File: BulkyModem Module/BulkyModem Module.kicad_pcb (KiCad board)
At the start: 2 copper layers, 100 x 100 mm, 93 parts, among them J1 DC IN, J2 DCE, J3 Module_Panel, J4 Conn_Power, J5 C64_Modem_IDC, K1 HK19F-DC, M1 Mounting, M2 Mounting, M3 Mounting, M4 Mounting, Q1 2N3904, Q4 2N3904, Q5 2N3904, Q6 2N3904, Q7 2N3904, Q8 2N3904, U1 74HCT244, U2 74HCT04, U3 MAX232, U4 MAX232, U5 74HCT04

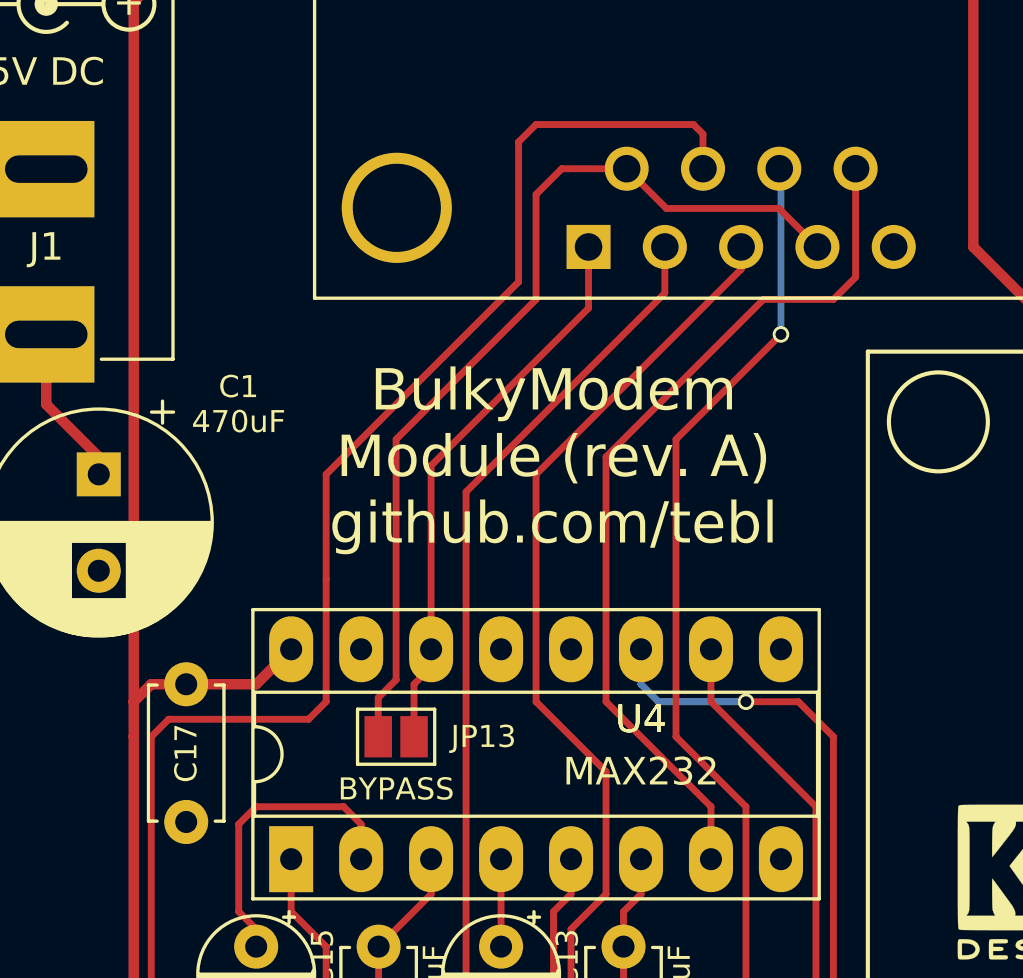
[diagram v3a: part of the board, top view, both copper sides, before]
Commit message: Tweak schematic in order to fix LEDs and default jumper settings moved to working configuration
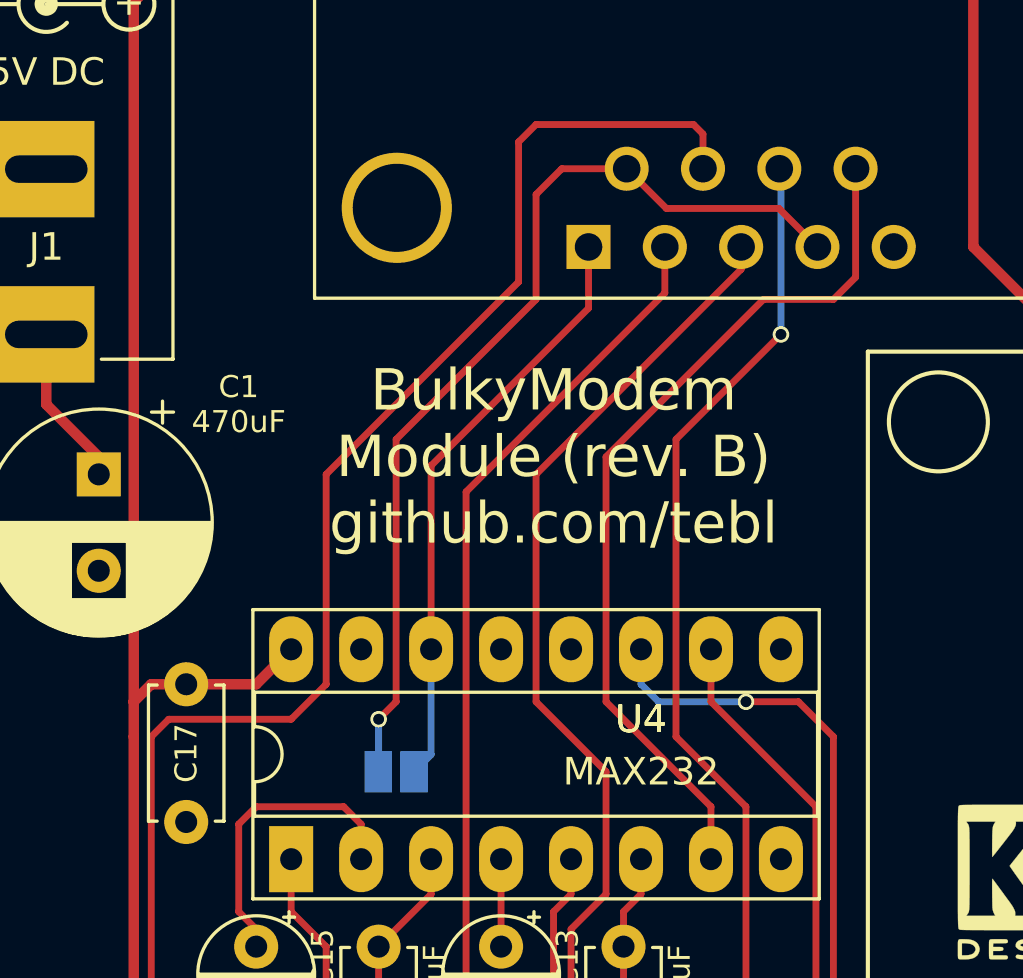
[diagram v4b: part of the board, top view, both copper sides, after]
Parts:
- JP13: moved to B.Cu
- moved JP13 1.27 mm to (95.9, 84.5)
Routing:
- net Net-(J2-Pad4): track 33.8 -> 35.1 mm, vias 0 -> 1
- net /RS-232/SER_DCD: track 20.4 -> 21.7 mm
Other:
- board text added: "BulkyModem Module (rev. B) github.com/tebl"
- board text removed: "BulkyModem Module (rev. A) github.com/tebl"
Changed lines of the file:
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@@
       (net 78 "Net-(JP12-Pad2)"))
   )
-  (module Jumper:SolderJumper-2_P1.3mm_Open_Pad1.0x1.5mm (layer F.Cu)
-    (at 95.885 83.185 180)
+  (module Jumper:SolderJumper-2_P1.3mm_Open_Pad1.0x1.5mm (layer B.Cu)
+    (at 95.885 84.455 180)
     (descr "SMD Solder Jumper, 1x1.5mm Pads, 0.3mm gap, open")
     (tags "solder jumper open")
     (attr virtual)
-    (fp_text reference JP13 (at -3.175 0) (layer F.SilkS)
-      (effects (font (size 0.8 0.8) (thickness 0.1)))
-    )
-    (fp_text value BYPASS (at 0 -1.905) (layer F.SilkS)
-      (effects (font (size 0.8 0.8) (thickness 0.1)))
-    )
-    (fp_line (start -1.4 1) (end -1.4 -1) (layer F.SilkS) (width 0.12))
-    (fp_line (start 1.4 1) (end -1.4 1) (layer F.SilkS) (width 0.12))
-    (fp_line (start 1.4 -1) (end 1.4 1) (layer F.SilkS) (width 0.12))
-    (fp_line (start -1.4 -1) (end 1.4 -1) (layer F.SilkS) (width 0.12))
-    (fp_line (start -1.65 -1.25) (end 1.65 -1.25) (layer F.CrtYd) (width 0.05))
-    (fp_line (start -1.65 -1.25) (end -1.65 1.25) (layer F.CrtYd) (width 0.05))
-    (fp_line (start 1.65 1.25) (end 1.65 -1.25) (layer F.CrtYd) (width 0.05))
-    (fp_line (start 1.65 1.25) (end -1.65 1.25) (layer F.CrtYd) (width 0.05))
-    (pad 2 smd rect (at 0.65 0 180) (size 1 1.5) (layers F.Cu F.Mask)
+    (fp_text reference JP13 (at -3.175 0) (layer B.SilkS)
+      (effects (font (size 0.8 0.8) (thickness 0.1)) (justify mirror))
+    )
+    (fp_text value BYPASS (at 0 1.905) (layer B.SilkS)
+      (effects (font (size 0.8 0.8) (thickness 0.1)) (justify mirror))
+    )
+    (fp_line (start -1.4 -1) (end -1.4 1) (layer B.SilkS) (width 0.12))
+    (fp_line (start 1.4 -1) (end -1.4 -1) (layer B.SilkS) (width 0.12))
+    (fp_line (start 1.4 1) (end 1.4 -1) (layer B.SilkS) (width 0.12))
+    (fp_line (start -1.4 1) (end 1.4 1) (layer B.SilkS) (width 0.12))
+    (fp_line (start -1.65 1.25) (end 1.65 1.25) (layer B.CrtYd) (width 0.05))
+    (fp_line (start -1.65 1.25) (end -1.65 -1.25) (layer B.CrtYd) (width 0.05))
+    (fp_line (start 1.65 -1.25) (end 1.65 1.25) (layer B.CrtYd) (width 0.05))
+    (fp_line (start 1.65 -1.25) (end -1.65 -1.25) (layer B.CrtYd) (width 0.05))
+    (pad 2 smd rect (at 0.65 0 180) (size 1 1.5) (layers B.Cu B.Mask)
       (net 76 "Net-(J2-Pad4)"))
-    (pad 1 smd rect (at -0.65 0 180) (size 1 1.5) (layers F.Cu F.Mask)
+    (pad 1 smd rect (at -0.65 0 180) (size 1 1.5) (layers B.Cu B.Mask)
       (net 75 /RS-232/SER_DCD))
   )
@@
     (effects (font (size 1 1) (thickness 0.15)))
   )
-  (gr_text "BulkyModem\nModule (rev. A)\ngithub.com/tebl" (at 101.6 73.025) (layer F.SilkS)
+  (gr_text "BulkyModem\nModule (rev. B)\ngithub.com/tebl" (at 101.6 73.025) (layer F.SilkS)
     (effects (font (size 1.5 1.5) (thickness 0.15)))
   )
@@
   (segment (start 102.235 90.17) (end 102.235 92.71) (width 0.25) (layer F.Cu) (net 36))
   (segment (start 108.41 65.405) (end 108.41 66.215) (width 0.25) (layer F.Cu) (net 36) (status 10))
-  (segment (start 107.025 62.565) (end 107.025 61.305) (width 0.25) (layer F.Cu) (net 37) (status 10))
-  (segment (start 107.025 61.305) (end 106.68 60.96) (width 0.25) (layer F.Cu) (net 37))
-  (segment (start 106.68 60.96) (end 100.965 60.96) (width 0.25) (layer F.Cu) (net 37))
-  (segment (start 100.965 60.96) (end 100.33 61.595) (width 0.25) (layer F.Cu) (net 37))
-  (segment (start 100.33 61.595) (end 100.33 66.675) (width 0.25) (layer F.Cu) (net 37))
-  (segment (start 100.33 66.675) (end 93.345 73.66) (width 0.25) (layer F.Cu) (net 37))
-  (segment (start 93.345 73.66) (end 93.345 77.47) (width 0.25) (layer F.Cu) (net 37))
-  (segment (start 93.345 77.47) (end 93.345 81.915) (width 0.25) (layer F.Cu) (net 37))
-  (segment (start 109.22 122.555) (end 109.22 121.285) (width 0.25) (layer F.Cu) (net 37) (status 20))
+  (segment (start 109.22 122.555) (end 109.22 121.285) (width 0.25) (layer F.Cu) (net 37))
   (segment (start 108.585 123.19) (end 109.22 122.555) (width 0.25) (layer F.Cu) (net 37))
   (segment (start 106.68 123.19) (end 108.585 123.19) (width 0.25) (layer F.Cu) (net 37))
   (segment (start 106.045 122.555) (end 106.68 123.19) (width 0.25) (layer F.Cu) (net 37))
+  (segment (start 93.98 109.22) (end 105.41 109.22) (width 0.25) (layer F.Cu) (net 37))
+  (segment (start 93.345 108.585) (end 93.98 109.22) (width 0.25) (layer F.Cu) (net 37))
+  (segment (start 93.345 105.41) (end 93.345 108.585) (width 0.25) (layer F.Cu) (net 37))
+  (segment (start 91.694 94.234) (end 92.71 95.25) (width 0.25) (layer F.Cu) (net 37))
+  (segment (start 107.025 61.305) (end 106.68 60.96) (width 0.25) (layer F.Cu) (net 37))
+  (segment (start 92.71 104.775) (end 93.345 105.41) (width 0.25) (layer F.Cu) (net 37))
+  (segment (start 100.33 61.595) (end 100.33 66.675) (width 0.25) (layer F.Cu) (net 37))
+  (segment (start 107.025 62.565) (end 107.025 61.305) (width 0.25) (layer F.Cu) (net 37))
+  (segment (start 93.345 81.28) (end 92.075 82.55) (width 0.25) (layer F.Cu) (net 37))
+  (segment (start 100.965 60.96) (end 100.33 61.595) (width 0.25) (layer F.Cu) (net 37))
+  (segment (start 106.68 60.96) (end 100.965 60.96) (width 0.25) (layer F.Cu) (net 37))
+  (segment (start 92.075 82.55) (end 87.63 82.55) (width 0.25) (layer F.Cu) (net 37))
+  (segment (start 105.41 109.22) (end 106.045 109.855) (width 0.25) (layer F.Cu) (net 37))
+  (segment (start 100.33 66.675) (end 93.345 73.66) (width 0.25) (layer F.Cu) (net 37))
+  (segment (start 93.345 73.66) (end 93.345 81.28) (width 0.25) (layer F.Cu) (net 37))
+  (segment (start 92.71 95.25) (end 92.71 104.775) (width 0.25) (layer F.Cu) (net 37))
+  (segment (start 87.63 82.55) (end 86.995 83.185) (width 0.25) (layer F.Cu) (net 37))
+  (segment (start 86.995 83.185) (end 86.995 93.345) (width 0.25) (layer F.Cu) (net 37))
+  (segment (start 87.884 94.234) (end 91.694 94.234) (width 0.25) (layer F.Cu) (net 37))
   (segment (start 106.045 109.855) (end 106.045 122.555) (width 0.25) (layer F.Cu) (net 37))
-  (segment (start 93.345 81.915) (end 92.71 82.55) (width 0.25) (layer F.Cu) (net 37))
-  (segment (start 93.345 105.41) (end 93.345 108.585) (width 0.25) (layer F.Cu) (net 37))
-  (segment (start 92.71 82.55) (end 87.63 82.55) (width 0.25) (layer F.Cu) (net 37))
-  (segment (start 86.995 83.185) (end 86.995 93.345) (width 0.25) (layer F.Cu) (net 37))
   (segment (start 86.995 93.345) (end 87.884 94.234) (width 0.25) (layer F.Cu) (net 37))
-  (segment (start 87.63 82.55) (end 86.995 83.185) (width 0.25) (layer F.Cu) (net 37))
-  (segment (start 91.694 94.234) (end 92.71 95.25) (width 0.25) (layer F.Cu) (net 37))
-  (segment (start 87.884 94.234) (end 91.694 94.234) (width 0.25) (layer F.Cu) (net 37))
-  (segment (start 92.71 95.25) (end 92.71 104.775) (width 0.25) (layer F.Cu) (net 37))
-  (segment (start 93.345 108.585) (end 93.98 109.22) (width 0.25) (layer F.Cu) (net 37))
-  (segment (start 92.71 104.775) (end 93.345 105.41) (width 0.25) (layer F.Cu) (net 37))
-  (segment (start 105.41 109.22) (end 106.045 109.855) (width 0.25) (layer F.Cu) (net 37))
-  (segment (start 93.98 109.22) (end 105.41 109.22) (width 0.25) (layer F.Cu) (net 37))
   (via (at 109.855 68.58) (size 0.6) (drill 0.4) (layers F.Cu B.Cu) (net 38))
   (segment (start 109.855 62.625) (end 109.795 62.565) (width 0.25) (layer B.Cu) (net 38) (status 30))
@@
   (segment (start 97.155 73.3425) (end 102.87 67.6275) (width 0.25) (layer F.Cu) (net 75))
   (segment (start 97.155 80.01) (end 97.155 73.3425) (width 0.25) (layer F.Cu) (net 75) (status 10))
-  (segment (start 97.155 80.66) (end 97.155 80.01) (width 0.25) (layer F.Cu) (net 75) (status 30))
-  (segment (start 96.535 81.28) (end 97.155 80.66) (width 0.25) (layer F.Cu) (net 75) (status 20))
-  (segment (start 96.535 81.28) (end 96.535 83.185) (width 0.25) (layer F.Cu) (net 75) (status 20))
+  (segment (start 97.155 83.835) (end 96.535 84.455) (width 0.25) (layer B.Cu) (net 75))
+  (segment (start 97.155 80.01) (end 97.155 83.835) (width 0.25) (layer B.Cu) (net 75))
   (segment (start 109.783 64.008) (end 111.18 65.405) (width 0.25) (layer F.Cu) (net 76) (status 20))
   (segment (start 105.698 64.008) (end 109.783 64.008) (width 0.25) (layer F.Cu) (net 76))
   (segment (start 104.255 62.565) (end 105.698 64.008) (width 0.25) (layer F.Cu) (net 76) (status 10))
-  (segment (start 101.9 62.565) (end 104.255 62.565) (width 0.25) (layer F.Cu) (net 76) (status 20))
-  (segment (start 100.965 63.5) (end 101.9 62.565) (width 0.25) (layer F.Cu) (net 76))
-  (segment (start 100.965 67.31) (end 100.965 63.5) (width 0.25) (layer F.Cu) (net 76))
-  (segment (start 95.885 72.39) (end 100.965 67.31) (width 0.25) (layer F.Cu) (net 76))
-  (segment (start 95.885 81.12125) (end 95.885 72.39) (width 0.25) (layer F.Cu) (net 76))
-  (segment (start 95.235 81.77125) (end 95.885 81.12125) (width 0.25) (layer F.Cu) (net 76))
-  (segment (start 95.235 83.185) (end 95.235 81.77125) (width 0.25) (layer F.Cu) (net 76) (status 10))
+  (via (at 95.25 82.55) (size 0.6) (drill 0.4) (layers F.Cu B.Cu) (net 76))
+  (segment (start 95.25 84.44) (end 95.235 84.455) (width 0.25) (layer B.Cu) (net 76))
+  (segment (start 95.25 82.55) (end 95.25 84.44) (width 0.25) (layer B.Cu) (net 76))
+  (segment (start 95.885 81.915) (end 95.25 82.55) (width 0.25) (layer F.Cu) (net 76))
+  (segment (start 95.885 72.39) (end 95.885 81.915) (width 0.25) (layer F.Cu) (net 76))
+  (segment (start 100.965 67.31) (end 95.885 72.39) (width 0.25) (layer F.Cu) (net 76))
+  (segment (start 100.965 63.5) (end 100.965 67.31) (width 0.25) (layer F.Cu) (net 76))
+  (segment (start 101.9 62.565) (end 100.965 63.5) (width 0.25) (layer F.Cu) (net 76))
+  (segment (start 104.255 62.565) (end 101.9 62.565) (width 0.25) (layer F.Cu) (net 76))
   (segment (start 129.57 106.65) (end 129.54 106.68) (width 0.25) (layer F.Cu) (net 77) (status 30))
   (segment (start 129.57 103.505) (end 129.57 106.65) (width 0.25) (layer F.Cu) (net 77) (status 30))

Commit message: Layout updated
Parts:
- removed C10, C11, C16, C20, C9: 22uF, Capacitor_THT:CP_Radial_D5.0mm_P2.00mm
- removed the G*** at (79.4, 113.0)
- removed J4: Conn_Power, BulkyModem:Conn_Power
- removed Q1, Q4, Q5, Q6, Q7, Q8: 2N3904, Package_TO_SOT_THT:TO-92_Inline_Wide
- removed R11, R13, R24, R7, R9: 10k, resistor:R_Axial_DIN0207_L6.3mm_D2.5mm_P10.16mm_Horizontal
- removed R22: 2k, resistor:R_Axial_DIN0207_L6.3mm_D2.5mm_P10.16mm_Horizontal
- removed R23: 1k, resistor:R_Axial_DIN0207_L6.3mm_D2.5mm_P10.16mm_Horizontal
- removed the REF*** at (122.6, 88.3)
- added D11: 1N5819, Diode_THT:D_DO-41_SOD81_P10.16mm_Horizontal, F.Cu at (90.2, 67.9)
- added D12: STANDBY, LED_THT:LED_D3.0mm, F.Cu at (79.4, 149.9)
- added D13: STANDBY, LED_THT:LED_D3.0mm, F.Cu at (73.4, 66.7)
- added G***: LOGO, artwork:BulkyModem_small, F.Cu at (95.2, 126.4)
- added JP15: TX_FILTER, Jumper:SolderJumper-3_P1.3mm_Open_RoundedPad1.0x1.5mm, F.Cu at (117.5, 88.9)
- added JP16: BYPASS, Jumper:SolderJumper-2_P1.3mm_Open_Pad1.0x1.5mm, F.Cu at (115.6, 127.6)
- added R3: 2k2, resistor:R_Axial_DIN0207_L6.3mm_D2.5mm_P10.16mm_Horizontal, F.Cu at (83.8, 92.1)
- added U6: 74HCT32, Package_DIP:DIP-14_W7.62mm_Socket_LongPads, F.Cu at (124.5, 132.1)
- C8: value 22uF -> 100nF; footprint Capacitor_THT:CP_Radial_D5.0mm_P2.00mm -> Capacitor_THT:C_Disc_D4.7mm_W2.5mm_P5.00mm
- JP3: value RxD_SEL -> SEL_RxD
- JP4: value TxD_SEL -> SEL_TxD
- JP5: value CTS_SEL -> SEL_CTS
- JP6: value RTS_SEL -> SEL_RTS
- JP7: value 232_EN -> 232_SW
- R1: value 10k -> 2k2
- R10, R12, R14, R2, R25, R8: value 470 -> 1k
- REF***: moved to F.Cu
- moved R1 79.0 mm to (72.4, 125.7), turned to 270 degrees
- moved JP1 28.6 mm to (74.3, 103.5), turned to 270 degrees
- moved REF*** 28.5 mm to (101.0, 71.1), turned to 0 degrees
- moved C8 26.7 mm to (120.7, 125.7), turned to 270 degrees
- moved G*** 22.5 mm to (94.6, 128.9), turned to 180 degrees
- moved R2 11.7 mm to (153.7, 124.5), turned to 270 degrees
- moved R16 9.55 mm to (157.5, 124.5)
- moved C19 6.02 mm to (132.7, 85.1)
- moved U1 6.02 mm to (136.5, 91.4)
- moved R15 5.75 mm to (149.9, 124.5)
- moved D2 5.08 mm to (84.5, 149.9)
- turned JP10 to 0 degrees
- turned JP8 to 0 degrees
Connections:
- A1 pad 18: ESP_TX -> Net-(A1-Pad18)
- A1 pad 23: Net-(A1-Pad23) -> ESP_RI
- A1 pad 26: Net-(A1-Pad26) -> ESP_DCD
- A1 pad 9: Net-(A1-Pad9) -> (no net)
- C8 pad 1: Net-(C8-Pad1) -> +5V
- J1 pad 1: VIN -> Net-(D11-Pad2)
- J3 pad 17: (no net) -> VSB
- J3 pad 4: (no net) -> /Front panel/LED_STB
- JP8 pad 1: Net-(JP8-Pad1) -> /232_TX
- JP8 pad 3: /232_TX -> Net-(JP8-Pad3)
- K1 pad 11: (no net) -> VSB
- R1 pad 1: Net-(Q1-Pad2) -> GND
- R1 pad 2: ESP_RI -> Net-(D12-Pad1)
- R10 pad 1: Net-(C9-Pad1) -> ESP_TX
- R12 pad 1: Net-(C10-Pad1) -> Net-(R12-Pad1)
- R14 pad 1: Net-(C11-Pad1) -> Net-(R14-Pad1)
- R2 pad 1: Net-(C20-Pad1) -> Net-(R2-Pad1)
- R25 pad 1: Net-(C16-Pad1) -> Net-(R25-Pad1)
- R8 pad 1: Net-(C8-Pad1) -> ESP_RX
- U2 pad 4: Net-(JP8-Pad1) -> Net-(JP8-Pad3)
- U2 pad 8: Net-(JP10-Pad1) -> Net-(JP10-Pad3)
- U2 pad 9: Net-(JP10-Pad3) -> Net-(JP10-Pad1)
- U3 pad 12: Net-(JP10-Pad3) -> Net-(JP10-Pad1)
- U5 pad 10: Net-(U5-Pad10) -> Net-(R2-Pad1)
- U5 pad 11: Net-(A1-Pad23) -> ESP_RI
- U5 pad 3: Net-(A1-Pad26) -> ESP_RTS
- U5 pad 4: Net-(U5-Pad4) -> Net-(R14-Pad1)
- U5 pad 5: Net-(U5-Pad4) -> ESP_CTS
- U5 pad 6: ESP_DCD -> Net-(R12-Pad1)
- U5 pad 8: ESP_RI -> Net-(R25-Pad1)
- U5 pad 9: Net-(U5-Pad10) -> ESP_DCD
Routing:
- net VSB: track 0.00 -> 168.8 mm, vias 0 -> 4
- net /Front panel/LED_STB: track 0.00 -> 140.1 mm, vias 0 -> 1
- net Net-(A1-Pad18): track 0.00 -> 102.5 mm, vias 0 -> 5
- net Net-(R14-Pad1): track 0.00 -> 90.3 mm, vias 0 -> 1
- net ESP_CTS: track 152.1 -> 67.9 mm
- net ESP_RTS: track 182.2 -> 100.4 mm, vias 3 -> 4
- net Net-(A1-Pad26): track 70.3 -> 0.00 mm, vias 4 -> 0
- net Net-(A1-Pad23): track 65.0 -> 0.00 mm, vias 1 -> 0
- net Net-(R12-Pad1): track 0.00 -> 63.6 mm
- net Net-(R25-Pad1): track 0.00 -> 59.8 mm
- net Net-(JP15-Pad2): track 0.00 -> 55.2 mm, vias 0 -> 2
- net Net-(A1-Pad27): track 5.08 -> 44.9 mm
- net Net-(JP10-Pad1): track 3.19 -> 42.3 mm, vias 0 -> 2
- net +5V: track 587.3 -> 548.3 mm, vias 2 -> 3
- net Net-(JP10-Pad3): track 41.3 -> 3.19 mm, vias 2 -> 0
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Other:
- board text added: "Licensed under CERN OHL v.1.2"
- board text added: "Module (rev. B) github.com/tebl"
- board text removed: "BulkyModem Module (rev. B) github.com/tebl"

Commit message: Alternate panel designs
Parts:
- R3, R4: value 2k2 -> 2k2*
- moved G*** 57.5 mm to (108.3, 73.0)

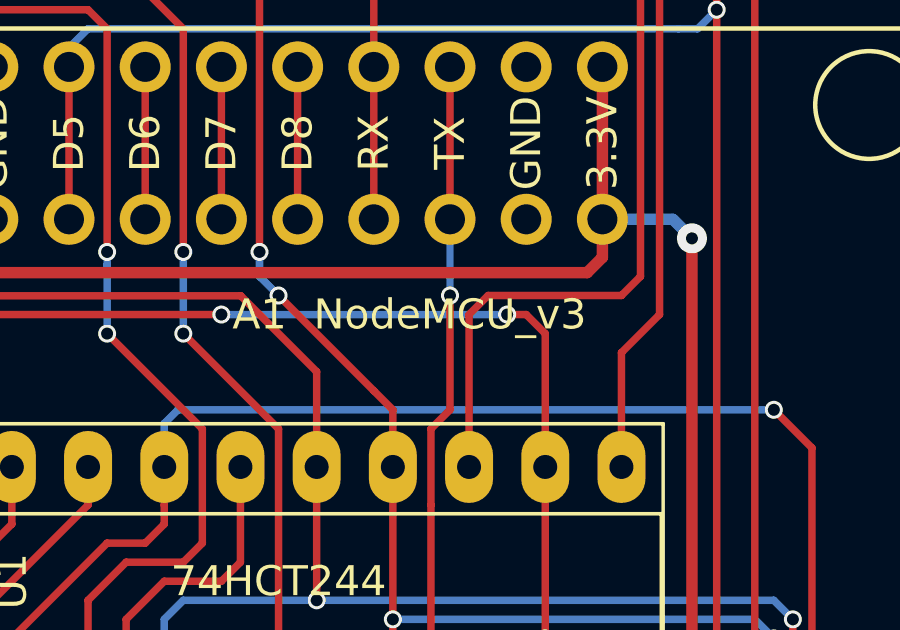
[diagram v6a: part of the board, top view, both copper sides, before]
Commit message: Updated UserPort layout
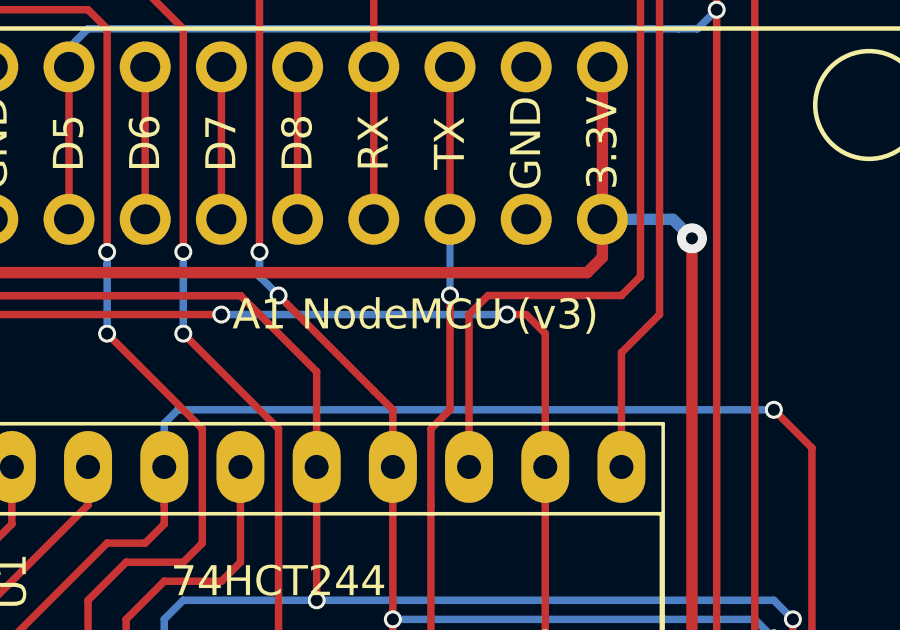
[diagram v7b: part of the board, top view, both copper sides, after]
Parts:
- A1: value NodeMCU_v3 -> NodeMCU (v3)
